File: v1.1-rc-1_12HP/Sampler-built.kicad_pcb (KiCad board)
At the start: 4 copper layers, 60.5 x 109.2 mm, 231 parts, among them J10 Eurorack_Power_10pin_Unshroud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, J11 3.5mm_Mono_Switched, J12 3.5mm_Mono_Switched, J13 3.5mm_Mono_Switched, J14 3.5mm_Mono_Switched, J15 3.5mm_Mono_Switched, J16 3.5mm_Mono_Switched, J17 3.5mm_Mono_Switched, J2 3.5mm_Mono_Switched, J3 Conn_01x04, J4 Conn_02x04, J6 3.5mm_Mono_Switched, J7 3.5mm_Mono_Switched, J8 3.5mm_Mono_Switched, J9 3.5mm_Mono_Switched, U1 TL072H, U10 TL072H, U11 TL072H, U12 TL072H, U13 AP62200WU-7, U14 TL072H, U15 NJM2068, U16 NJM2068, U2 STM32F746IE, U3 TL072H, U4 SDRAM_IS42S16400J-6BLI-TR, U5 TL072H, U6 NCP51460SN33, U8 TL072H, U9 PCM3060PW, Y1 16MHz_18pF_FA238

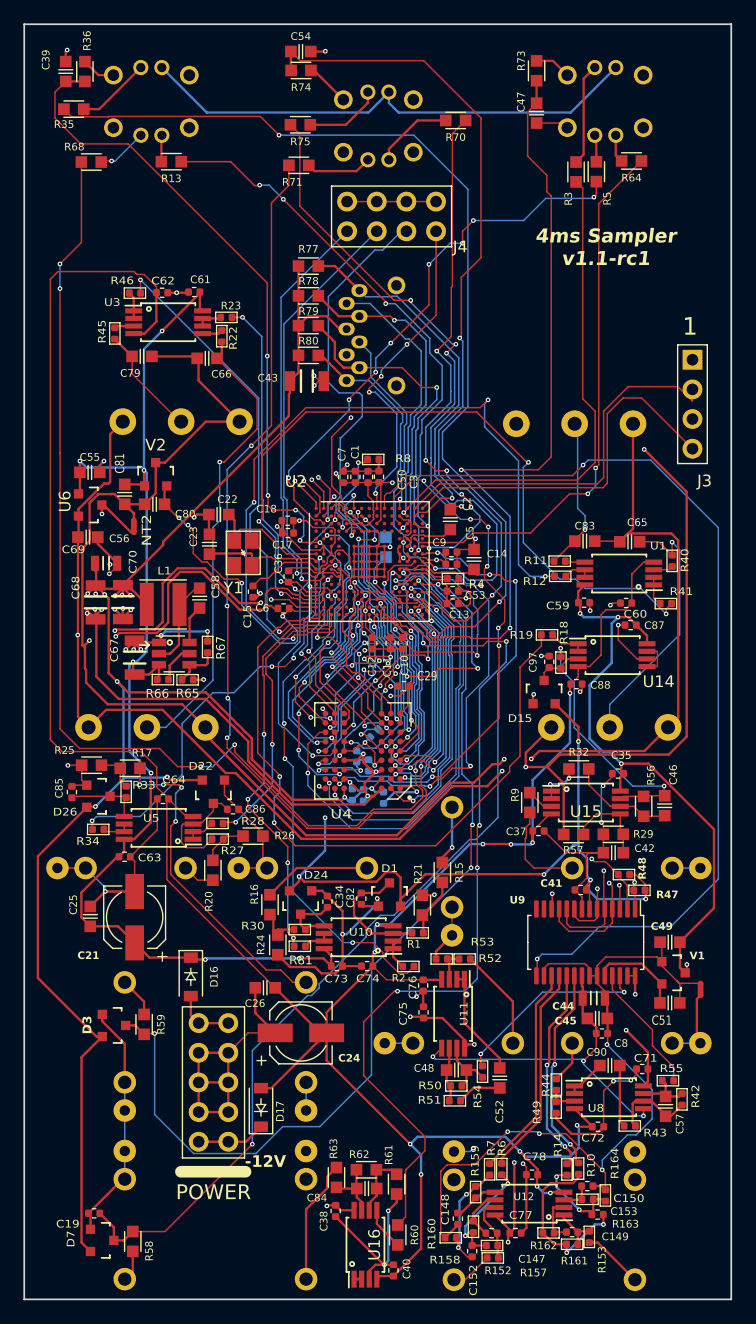
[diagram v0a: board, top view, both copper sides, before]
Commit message: Routing: Moved all digital traces under START POT to blue layer
Simplified lots of digital routing in that area
Made analog routing more strictly stay on red side
Moved VREF/GNDADC connection to ARM away from inductor
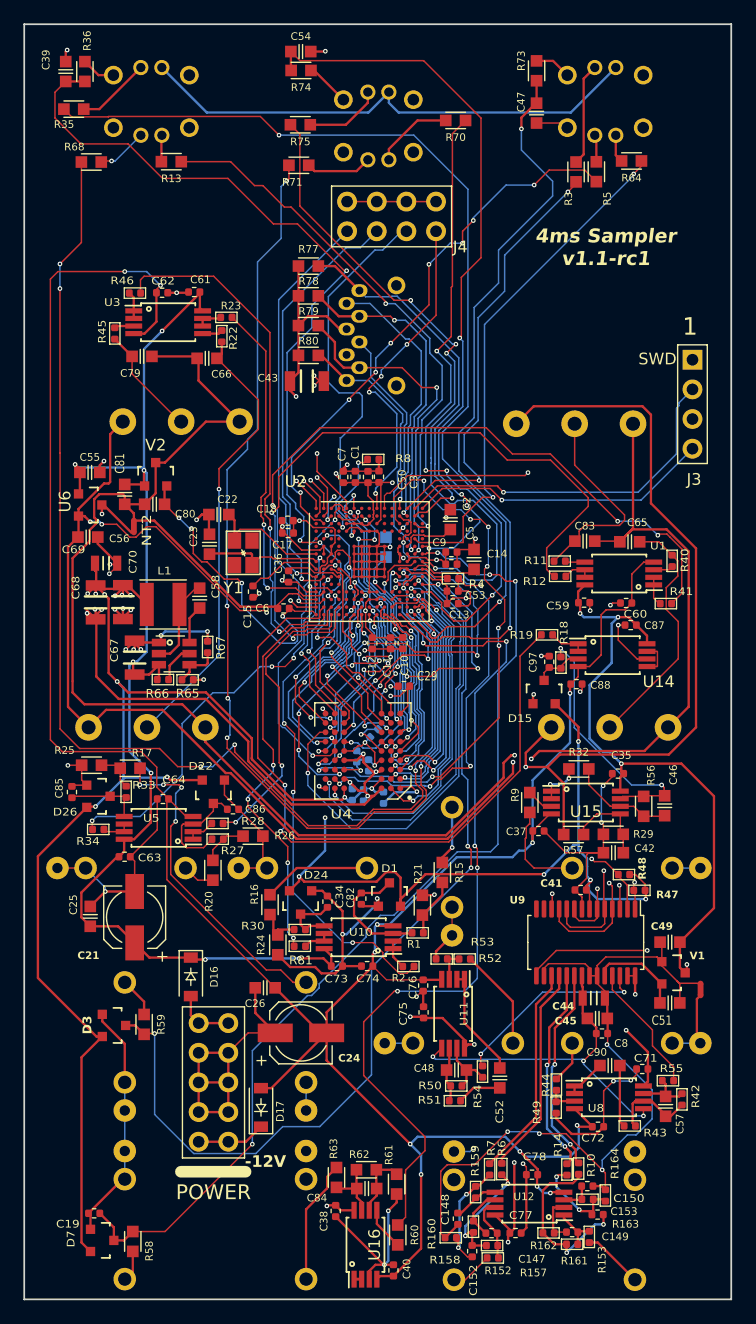
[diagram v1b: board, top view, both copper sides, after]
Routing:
- net +3V3: track 387.2 -> 400.3 mm, vias 30 -> 31
- net /I2C1_SDA: track 59.9 -> 69.6 mm
- net /CODEC_RESET: track 83.2 -> 74.3 mm
- net /A6: track 61.9 -> 69.5 mm, vias 6 -> 4
- net /SWDIO: track 32.3 -> 26.1 mm, vias 0 -> 1
- net /SAI_SD_A: track 66.2 -> 72.2 mm
- net /A7: track 65.9 -> 60.2 mm
- net /A1: track 65.1 -> 59.8 mm, vias 4 -> 2
- net /D0: track 42.4 -> 37.2 mm, vias 0 -> 2
- net Net-(POT_PITCH1-Center): track 12.3 -> 17.3 mm, vias 1 -> 0
- net GNDADC: track 168.6 -> 164.0 mm, vias 4 -> 2
- net /SAI_SCK: track 71.4 -> 75.9 mm
- net VREF+: track 163.3 -> 167.8 mm, vias 7 -> 6
- net /A9: track 41.4 -> 45.4 mm
- net /SAI_MCLK: track 69.4 -> 73.1 mm
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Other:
- board text added: "SWD"

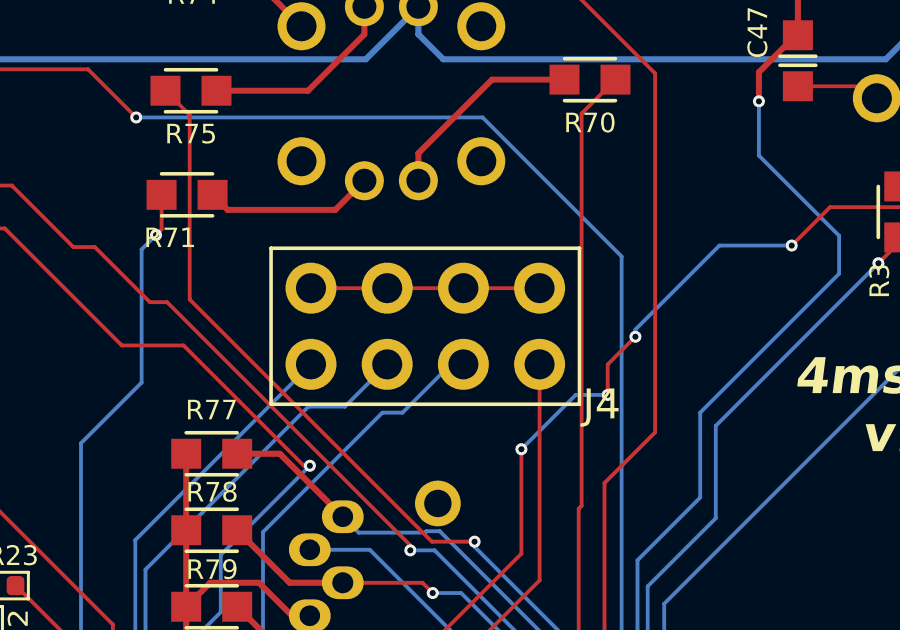
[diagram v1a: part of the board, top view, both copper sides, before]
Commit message: PCB: Fixed copper pour glitch, reconnected 3.3v, added Screen to silk and resolved DRC
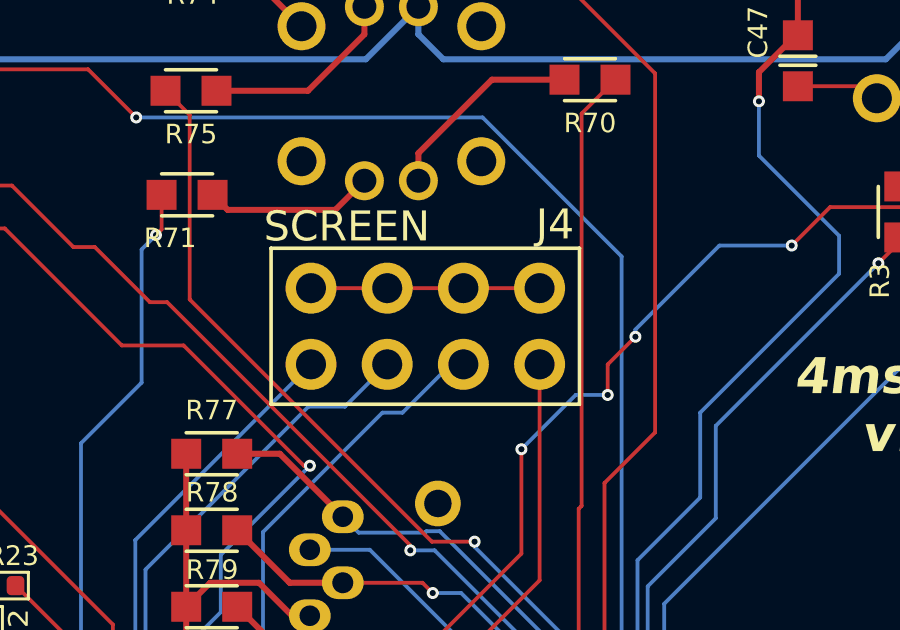
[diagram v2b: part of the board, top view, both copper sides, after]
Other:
- board text added: "SCREEN"
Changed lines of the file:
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@@
     (property "ki_keywords" "Conn_02x04")
     (attr through_hole)
-    (fp_text reference "J4" (at -2.609922 5.883352 180) (layer "F.SilkS")
+    (fp_text reference "J4" (at 3.390078 4.323352 180) (layer "F.SilkS")
         (effects (font (size 1 1) (thickness 0.1905)))
     )
@@
     )
   )
+  (gr_text "SCREEN" (at 161.72 30.05) (layer "F.SilkS")
+    (effects (font (size 1 1) (thickness 0.15)) (justify left bottom))
+  )
   (gr_text "SWD" (at 188.24 45.58) (layer "F.SilkS")
     (effects (font (size 1 1) (thickness 0.15)) (justify left bottom))
@@
         (xy 139.710852 61.673023)
         (xy 139.926885 72.940838)
-        (xy 265.966932 73.540078)
+        (xy 139.92 73.67)
         (xy 158.846648 73.540078)
       )

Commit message: SCH: Replaced NJMs with 072Hs - PCB: updated PCB from schematic
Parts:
- U15, U16: value NJM2068 -> TL072H
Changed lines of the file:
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@@
     (descr "8-Lead Plastic Thin Shrink Small Outline (ST)-4.4 mm Body [TSSOP] (see Microchip Packaging Specification 00000049BS.pdf)")
     (tags "SSOP 0.65")
-    (property "JLCPCB ID" "")
-    (property "Manufacturer" "NJR")
-    (property "Part Number" "NJM2068V-TE1")
+    (property "JLCPCB ID" "C4370341")
+    (property "Manufacturer" "Texas Instruments")
+    (property "Part Number" "TL072HIPWR")
     (property "Production Stage" "A")
     (property "Sheetfile" "Sampler-built.kicad_sch")
     (property "Sheetname" "")
-    (property "Specifications" "NJM2068 Dual Opamp")
-    (property "ki_description" "NJM2068 Dual Opamp")
-    (property "ki_keywords" "NJM2068")
+    (property "Specifications" "Dual Opamp TSSOP-8")
+    (property "ki_description" "TL072 Dual Opamp TSSOP-8")
+    (property "ki_keywords" "TL072 TSSOP-8")
     (attr smd)
     (fp_text reference "U15" (at 0 0.775) (layer "F.SilkS")
         (effects (font (size 1 1) (thickness 0.15)))
     )
-    (fp_text value "NJM2068" (at 0 -0.725) (layer "F.Fab")
+    (fp_text value "TL072H" (at 0 -0.725) (layer "F.Fab")
         (effects (font (size 1 1) (thickness 0.15)))
     )
@@
     (tags "BGA 201 0.65")
     (property "Manufacturer" "STMicroelectronics")
-    (property "Part Number" "STM32F746IEK6")
+    (property "Part Number" "STM32F746IE")
     (property "Production Stage" "A")
     (property "Sheetfile" "Sampler-built.kicad_sch")
     (property "Sheetname" "")
-    (property "Specifications" "ARM Cortex-M7, KB flash, 256KB RAM, 216MHz, UFBGA-176")
+    (property "Specifications" "ARM Cortex-M7, 64KB flash, 256KB RAM, 216MHz, UFBGA-176")
     (property "ki_description" "ARM Cortex-M7, 64KB flash, 256KB RAM, 216MHz, UFBGA-176")
-    (property "ki_keywords" "ARM Cortex-M7 STM32F7 STM32F730")
+    (property "ki_keywords" "ARM Cortex-M7 STM32F746IE")
     (clearance 0.099822)
     (attr smd)
@@
     (descr "8-Lead Plastic Thin Shrink Small Outline (ST)-4.4 mm Body [TSSOP] (see Microchip Packaging Specification 00000049BS.pdf)")
     (tags "SSOP 0.65")
-    (property "JLCPCB ID" "")
-    (property "Manufacturer" "NJR")
-    (property "Part Number" "NJM2068V-TE1")
+    (property "JLCPCB ID" "C4370341")
+    (property "Manufacturer" "Texas Instruments")
+    (property "Part Number" "TL072HIPWR")
     (property "Production Stage" "A")
     (property "Sheetfile" "Sampler-built.kicad_sch")
     (property "Sheetname" "")
-    (property "Specifications" "NJM2068 Dual Opamp")
-    (property "ki_description" "NJM2068 Dual Opamp")
-    (property "ki_keywords" "NJM2068")
+    (property "Specifications" "Dual Opamp TSSOP-8")
+    (property "ki_description" "TL072 Dual Opamp TSSOP-8")
+    (property "ki_keywords" "TL072 TSSOP-8")
     (attr smd)
     (fp_text reference "U16" (at 0 0.775 90) (layer "F.SilkS")
         (effects (font (size 1 1) (thickness 0.15)))
     )
-    (fp_text value "NJM2068" (at 0 -0.725 90) (layer "F.Fab")
+    (fp_text value "TL072H" (at 0 -0.725 90) (layer "F.Fab")
         (effects (font (size 1 1) (thickness 0.15)))
     )
@@
     (tags "SOT-23")
     (property "Display" "5.0V, 150mA")
+    (property "JLCPCB ID" "C50754")
+    (property "JLCPCB ID 2" "C512090")
+    (property "JLCPCB ID 3" "C625398")
     (property "Manufacturer" "Diodes Incorporated")
     (property "Part Number" "AP2120N-5.0TRG1")
